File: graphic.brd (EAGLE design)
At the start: 109 x 29.5 mm, 82 parts, among them IC1 NE5532D, IC2 NE5532D, IC3 NE5532D, IC4 NE5532D, IC5 NE5532D

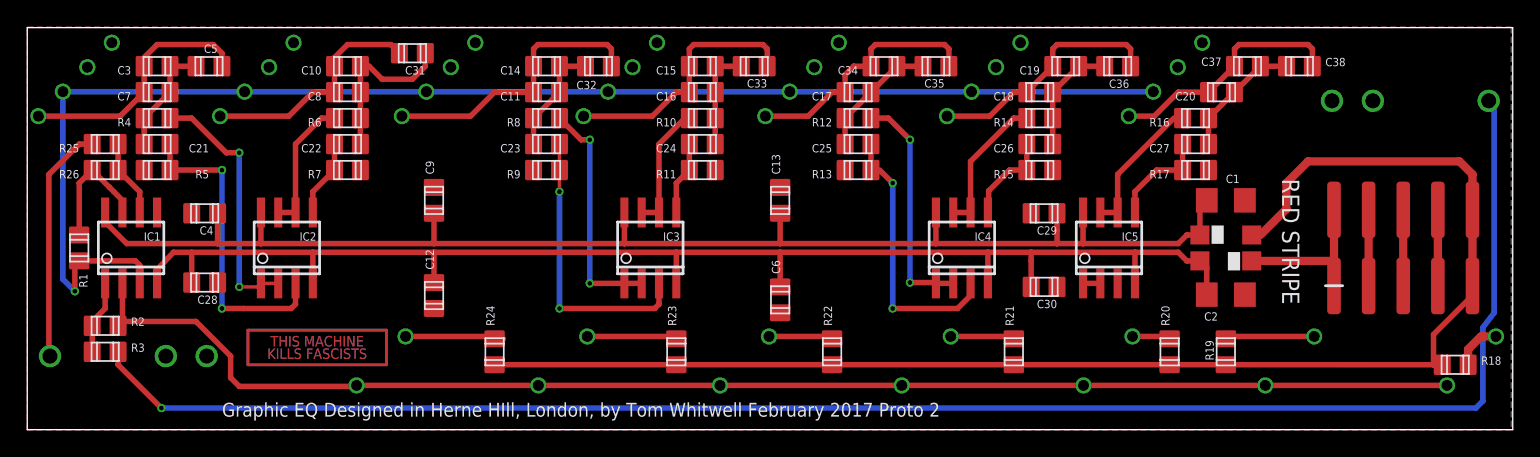
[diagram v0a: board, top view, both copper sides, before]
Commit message: Revision 1 board finalised - moved one resistor + added Fiducials
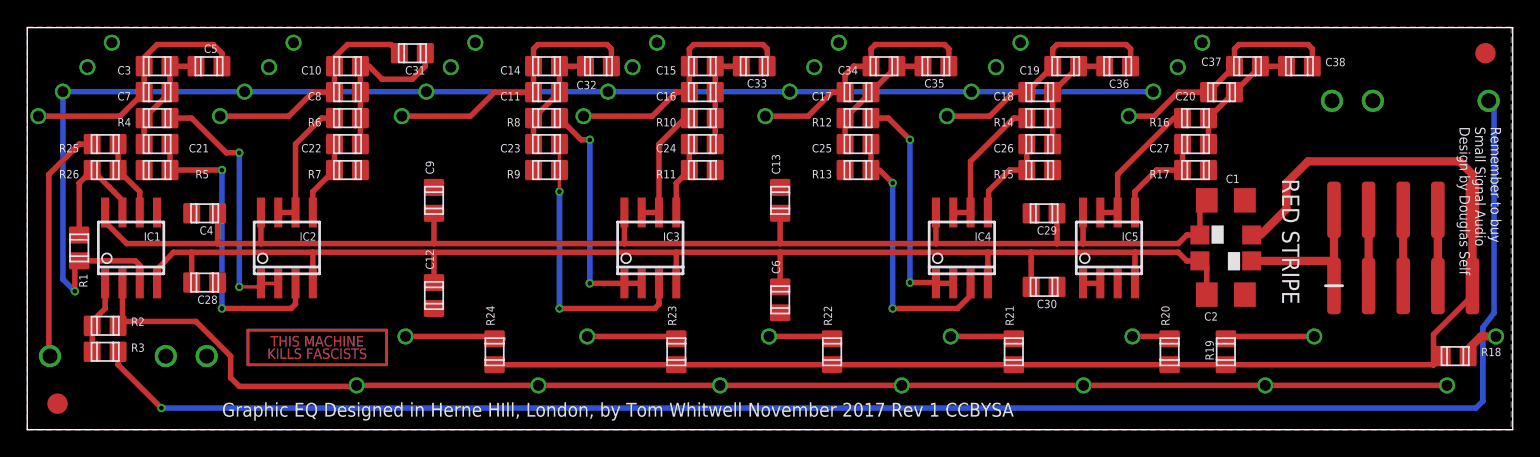
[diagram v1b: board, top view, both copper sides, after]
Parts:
- added FID1, FID2: FIDUCIAL1.5X3, SparkFun-Aesthetics:FIDUCIAL-1.5X3
- moved R18 0.63 mm to (104.8, 5.40)
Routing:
- net N$10: track 3.57 -> 2.93 mm
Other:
- board text added: "Graphic EQ Designed in Herne HIll, London, by Tom Whitwell November 2017 Rev 1 CCBYSA"
- board text added: "Remember to buy Small Signal Audio Design by Douglas Self"
- board text removed: "Graphic EQ Designed in Herne HIll, London, by Tom Whitwell February 2017 Proto 2"
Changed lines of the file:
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@@
 <?xml version="1.0" encoding="utf-8"?>
 <!DOCTYPE eagle SYSTEM "eagle.dtd">
-<eagle version="7.2.0">
+<eagle version="7.7.0">
 <drawing>
 <settings>
@@
 <grid distance="12.5" unitdist="mil" unit="mil" style="lines" multiple="1" display="no" altdistance="5" altunitdist="mil" altunit="mil"/>
 <layers>
-<layer number="1" name="Top" color="4" fill="1" visible="no" active="yes"/>
+<layer number="1" name="Top" color="4" fill="1" visible="yes" active="yes"/>
 <layer number="2" name="Route2" color="1" fill="3" visible="no" active="no"/>
 <layer number="3" name="Route3" color="4" fill="3" visible="no" active="no"/>
@@
 <layer number="15" name="Route15" color="4" fill="6" visible="no" active="no"/>
 <layer number="16" name="Bottom" color="1" fill="1" visible="no" active="yes"/>
-<layer number="17" name="Pads" color="2" fill="1" visible="no" active="yes"/>
-<layer number="18" name="Vias" color="2" fill="1" visible="no" active="yes"/>
+<layer number="17" name="Pads" color="2" fill="1" visible="yes" active="yes"/>
+<layer number="18" name="Vias" color="2" fill="1" visible="yes" active="yes"/>
 <layer number="19" name="Unrouted" color="6" fill="1" visible="no" active="yes"/>
-<layer number="20" name="Dimension" color="15" fill="1" visible="no" active="yes"/>
-<layer number="21" name="tPlace" color="7" fill="1" visible="no" active="yes"/>
-<layer number="22" name="bPlace" color="7" fill="1" visible="yes" active="yes"/>
+<layer number="20" name="Dimension" color="15" fill="1" visible="yes" active="yes"/>
+<layer number="21" name="tPlace" color="7" fill="1" visible="yes" active="yes"/>
+<layer number="22" name="bPlace" color="7" fill="1" visible="no" active="yes"/>
 <layer number="23" name="tOrigins" color="15" fill="1" visible="no" active="yes"/>
-<layer number="24" name="bOrigins" color="15" fill="1" visible="yes" active="yes"/>
+<layer number="24" name="bOrigins" color="15" fill="1" visible="no" active="yes"/>
 <layer number="25" name="tNames" color="7" fill="1" visible="no" active="yes"/>
 <layer number="26" name="bNames" color="7" fill="1" visible="no" active="yes"/>
@@
 <layer number="50" name="dxf" color="7" fill="1" visible="no" active="no"/>
 <layer number="51" name="tDocu" color="7" fill="1" visible="no" active="yes"/>
-<layer number="52" name="bDocu" color="7" fill="1" visible="yes" active="yes"/>
+<layer number="52" name="bDocu" color="7" fill="1" visible="no" active="yes"/>
 <layer number="53" name="tGND_GNDA" color="7" fill="9" visible="no" active="no"/>
 <layer number="54" name="bGND_GNDA" color="1" fill="9" visible="no" active="no"/>
@@
 75ml placement grid
 12.5mil routing grid</text>
-<text x="14.2875" y="0.9525" size="1.016" layer="21">Graphic EQ Designed in Herne HIll, London, by Tom Whitwell February 2017 Proto 2</text>
+<text x="14.2875" y="0.9525" size="1.016" layer="21">Graphic EQ Designed in Herne HIll, London, by Tom Whitwell November 2017 Rev 1 CCBYSA </text>
+<text x="105.0925" y="22.225" size="0.762" layer="21" rot="SR270">Remember to buy
+Small Signal Audio
+Design by Douglas Self</text>
 </plain>
 <attributes>
@@
 <element name="R16" library="we-rcl" package="C0805" value="1.8k" x="85.725" y="22.86" rot="R90"/>
 <element name="R17" library="we-rcl" package="C0805" value="51k" x="85.725" y="19.05" rot="R90"/>
-<element name="R18" library="we-rcl" package="C0805" value="2k" x="104.775" y="4.7625" rot="R270"/>
+<element name="R18" library="we-rcl" package="C0805" value="2k" x="104.775" y="5.3975" rot="R270"/>
 <element name="R19" library="we-rcl" package="C0805" value="2k" x="87.9475" y="5.715" smashed="yes">
 <attribute name="NAME" x="87.0585" y="5.08" size="0.6096" layer="25" font="vector" ratio="10" rot="R270" align="top-right"/>
@@
 <element name="C38" library="we-rcl" package="C0805" value="NP" x="93.345" y="26.67" rot="R270"/>
 <element name="U$1" library="MusicThingModular" package="TMKF" value="" x="21.2725" y="6.0325"/>
+<element name="FID1" library="SparkFun-Aesthetics" package="FIDUCIAL-1.5X3" value="FIDUCIAL1.5X3" x="2.2225" y="1.905"/>
+<element name="FID2" library="SparkFun-Aesthetics" package="FIDUCIAL-1.5X3" value="FIDUCIAL1.5X3" x="106.9975" y="27.6225"/>
 </elements>
 <signals>
@@
 <contactref element="R18" pad="2"/>
 <contactref element="R21" pad="2"/>
-<wire x1="103.825" y1="4.7625" x2="103.1874" y2="4.7626" width="0.4064" layer="1"/>
+<wire x1="103.825" y1="5.3975" x2="103.1874" y2="4.7626" width="0.4064" layer="1"/>
 <wire x1="103.1874" y1="4.7626" x2="87.9475" y2="4.765" width="0.4064" layer="1"/>
 <wire x1="83.82" y1="4.765" x2="87.9475" y2="4.765" width="0.4064" layer="1"/>
@@
 <contactref element="R18" pad="1"/>
 <contactref element="16KHZ" pad="B"/>
-<wire x1="105.725" y1="4.7625" x2="105.725" y2="5.898653125" width="0.6096" layer="1"/>
+<wire x1="105.725" y1="5.3975" x2="105.725" y2="5.898653125" width="0.6096" layer="1"/>
 <wire x1="107.767884375" y1="6.84026875" x2="106.666615625" y2="6.84026875" width="0.6096" layer="1"/>
 <wire x1="106.666615625" y1="6.84026875" x2="105.725" y2="5.898653125" width="0.6096" layer="1"/>
